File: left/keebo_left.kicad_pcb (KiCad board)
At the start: 2 copper layers, 147.6 x 114.3 mm, 58 parts, among them SW1 SW_Push, SW10 SW_Push, SW11 SW_Push, SW12 SW_Push, SW13 SW_Push, SW14 SW_Push, SW17 SW_Push, SW18 SW_Push, SW19 SW_Push, SW2 SW_Push, SW20 SW_Push, SW21 SW_Push, SW22 SW_Push, SW25 SW_Push, SW26 SW_Push, SW27 SW_Push, SW28 SW_Push, SW29 SW_Push, SW3 SW_Push, SW30 SW_Push, SW34 SW_Push, SW35 SW_Push, SW36 SW_Push, SW4 SW_Push, SW5 SW_Push, SW6 SW_Push, SW7 SW_Push, SW9 SW_Push, U1 nRF24L01_module, U2 keyplus_mini

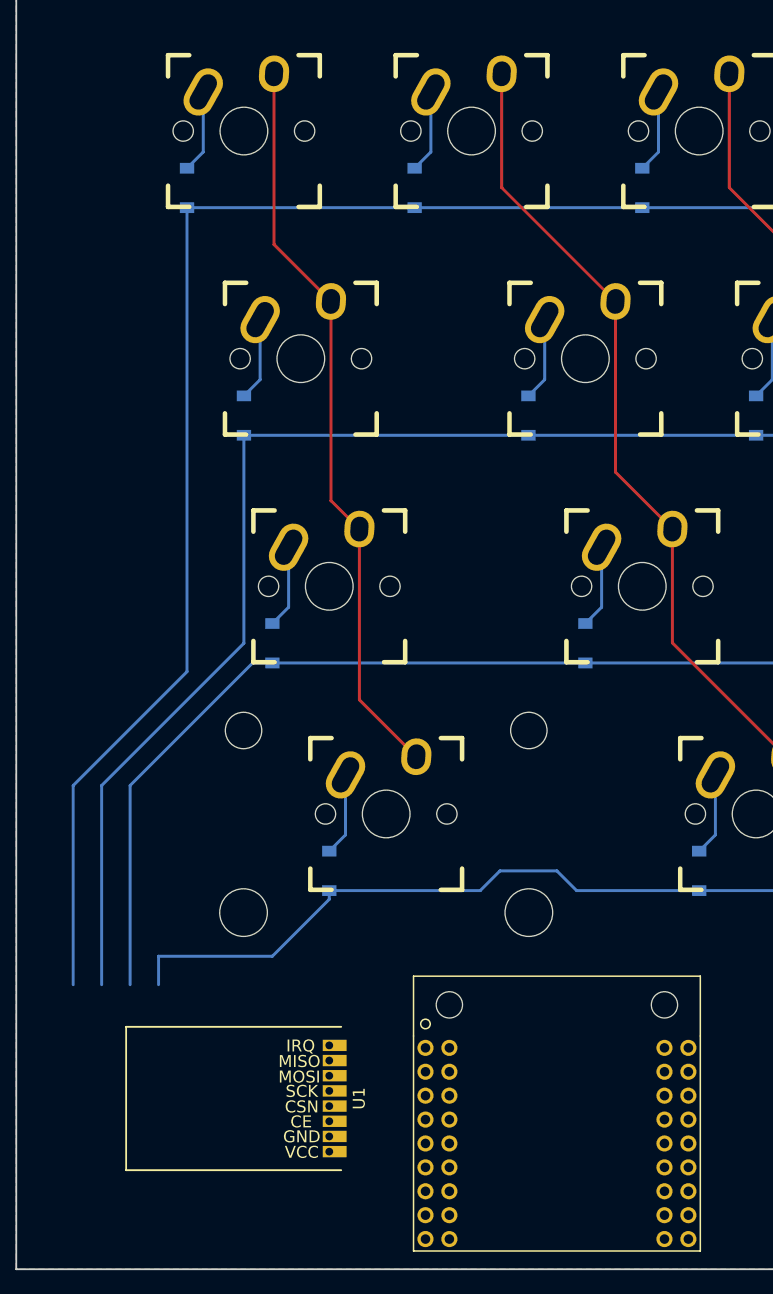
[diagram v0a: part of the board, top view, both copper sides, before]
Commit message: Make dependencies use relative path
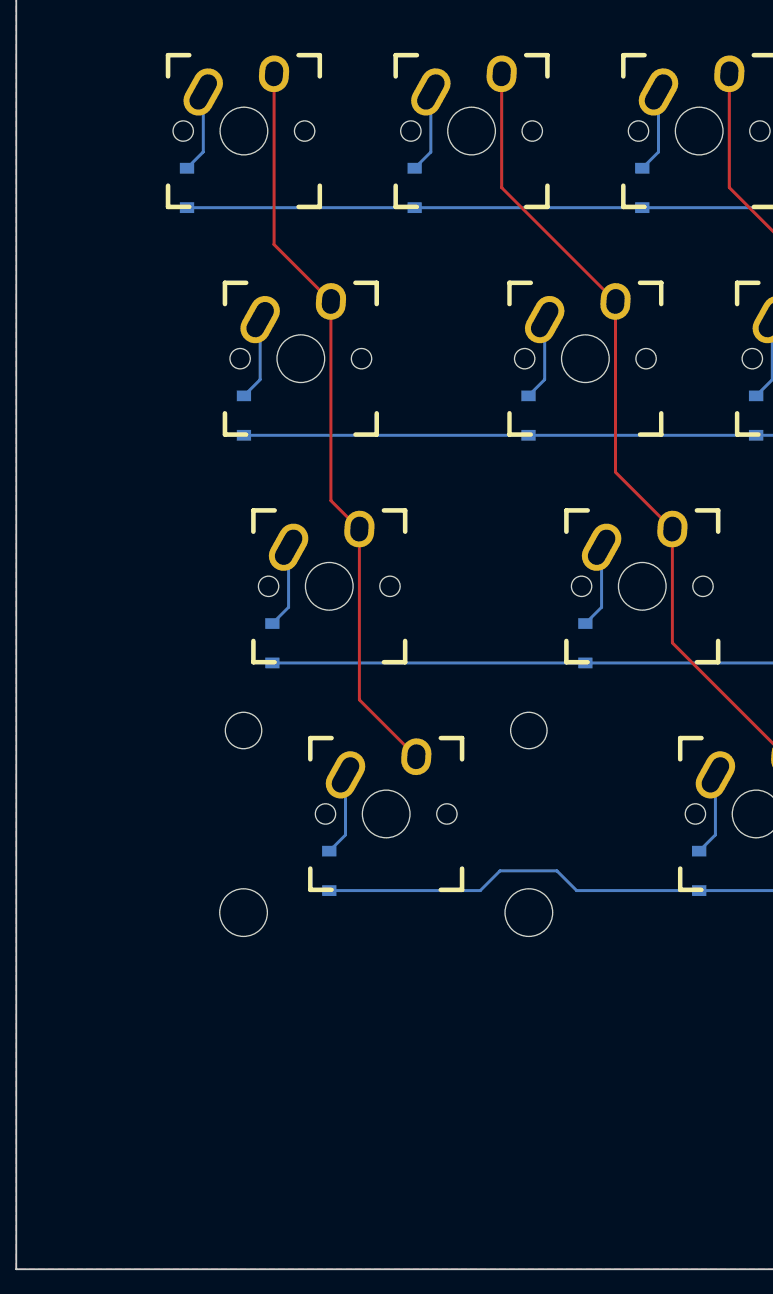
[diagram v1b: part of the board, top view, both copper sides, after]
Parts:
- removed U1: nRF24L01_module, nordic:NRF24L01-Module-SMD-TH
- removed U2: keyplus_mini, keyplus:keyplus_mini_v3
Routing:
- net /row0: track 183.3 -> 114.3 mm
- net /row1: track 150.9 -> 100.0 mm
- net /row2: track 135.2 -> 102.4 mm
- net /row3: track 127.9 -> 108.5 mm

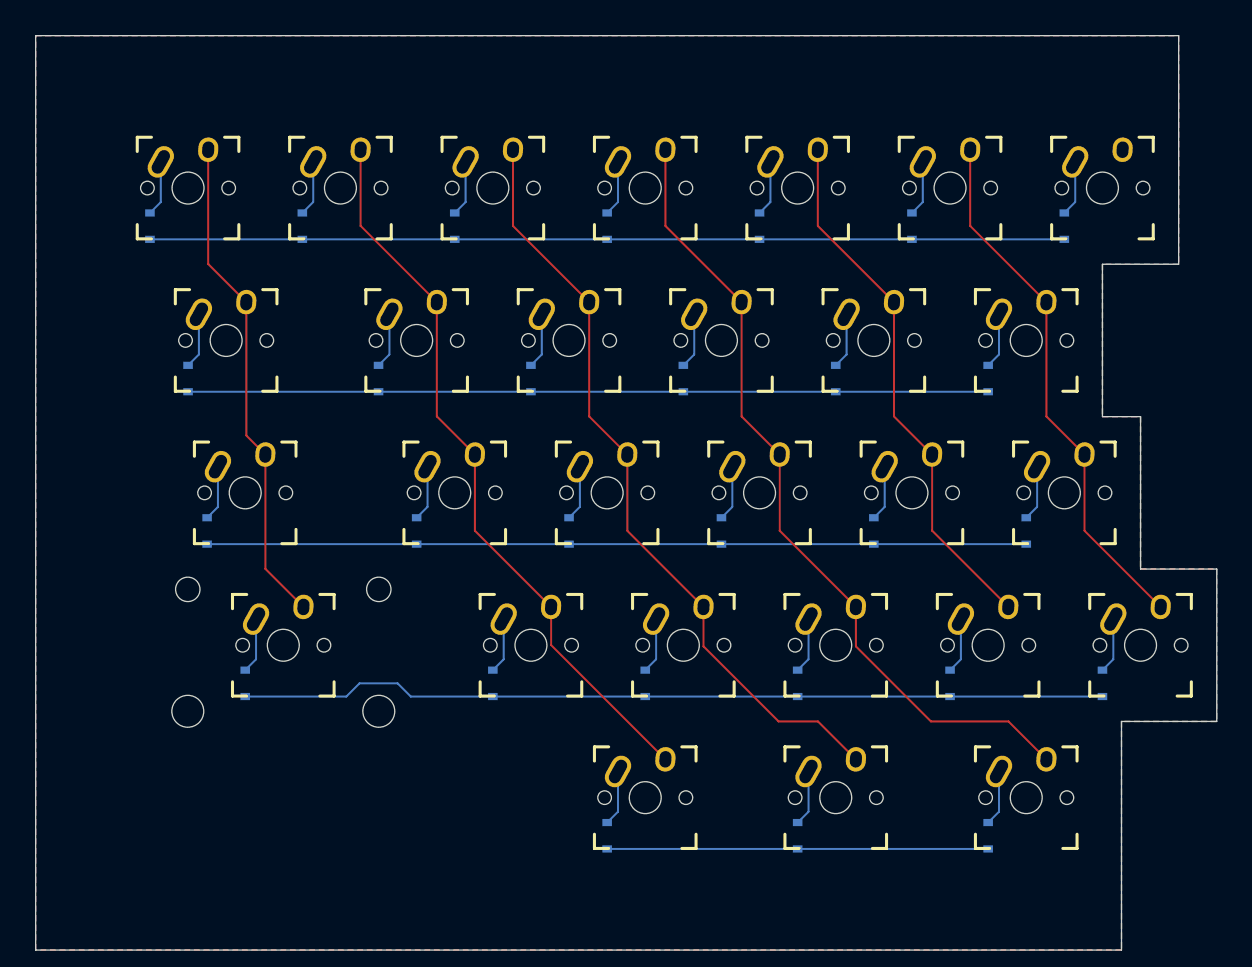
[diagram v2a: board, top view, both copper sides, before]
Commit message: Create PCB for low profile switches
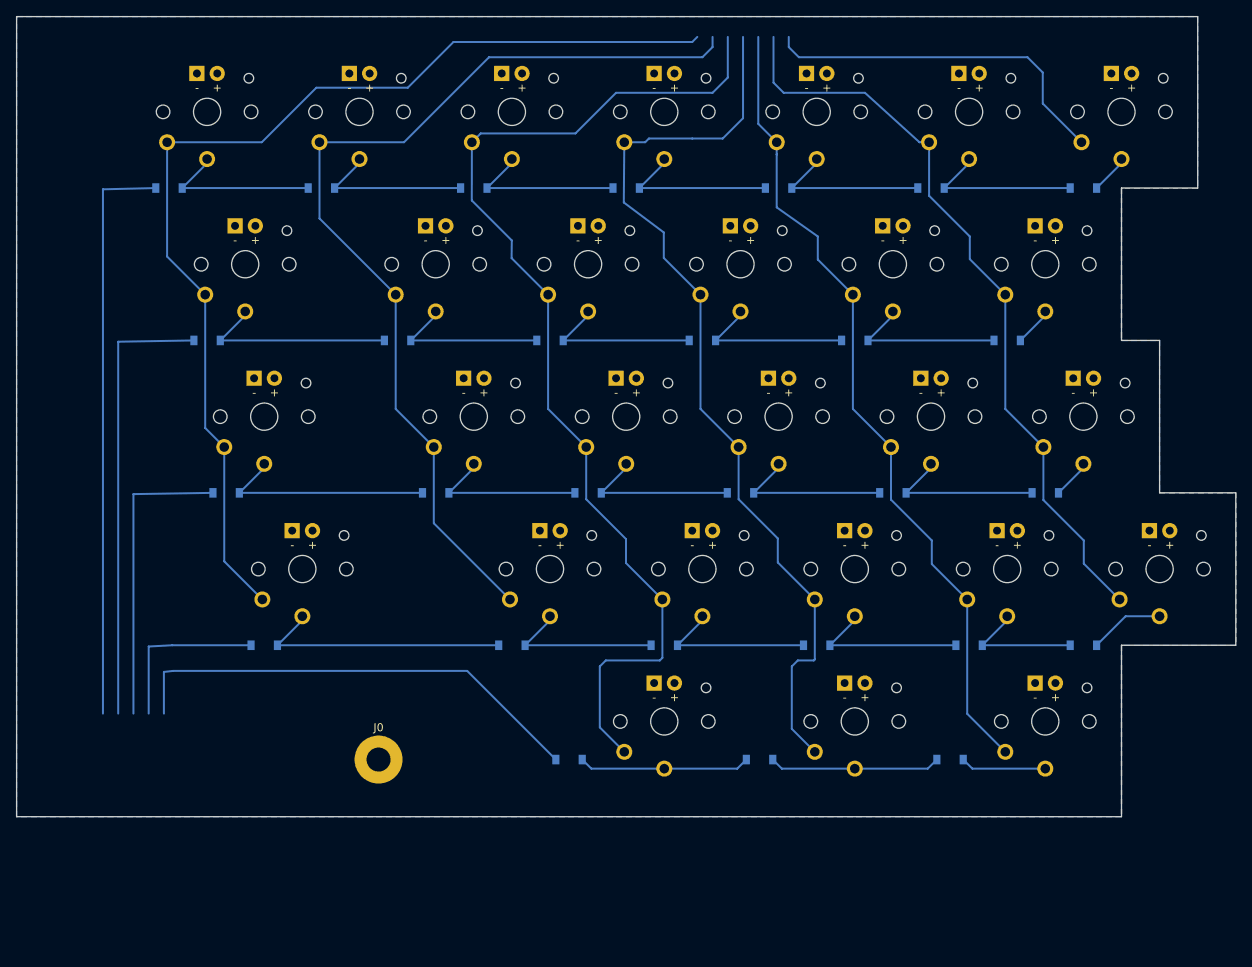
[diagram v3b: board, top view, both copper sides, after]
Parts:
- removed D34: 1N4148, Diodes_SMD:D_SOD-123
- removed SW34: SW_Push, keebs:Mx_Alps_125
- added D37: 1N4148, Diodes_SMD:D_SOD-123, B.Cu at (135.7, 111.9)
- added J0: Conn_01x01, Mounting_Holes:MountingHole_3mm_Pad, F.Cu at (64.3, 111.9)
- added SW37: SW_Push, req:Kailh-PG1350-1u, F.Cu at (147.6, 107.2)
- SW1, SW10, SW11, SW12, SW13, SW14, SW18, SW19, SW2, SW20, SW21, SW22, SW26, SW27, SW28, SW29, SW3, SW30, SW4, SW5, SW6, SW7: footprint keebs:Mx_Alps_100 -> req:Kailh-PG1350-1u
- SW17: footprint keebs:Mx_Alps_175 -> req:Kailh-PG1350-1u
- SW25: footprint keebs:Mx_Alps_225 -> req:Kailh-PG1350-1u
- SW35, SW36: footprint keebs:Mx_Alps_125 -> req:Kailh-PG1350-1u
- SW9: footprint keebs:Mx_Alps_150 -> req:Kailh-PG1350-1u
- moved D35 30.1 mm to (88.1, 111.9), turned to 0 degrees
- moved D36 30.1 mm to (111.9, 111.9), turned to 0 degrees
- moved SW35 23.5 mm to (100.0, 107.2)
- moved SW36 23.5 mm to (123.8, 107.2)
- moved SW6 9.82 mm to (138.1, 31.0)
- moved SW3 9.82 mm to (81.0, 31.0)
- moved SW4 9.82 mm to (100.0, 31.0)
- moved SW13 9.82 mm to (128.6, 50.0)
- moved SW2 9.82 mm to (61.9, 31.0)
- moved SW1 9.82 mm to (42.9, 31.0)
- moved SW5 9.82 mm to (119.1, 31.0)
- moved SW7 9.82 mm to (157.2, 31.0)
- moved SW30 9.82 mm to (161.9, 88.1)
- moved SW9 9.82 mm to (47.6, 50.0)
- moved SW10 9.82 mm to (71.4, 50.0)
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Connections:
- D1 pad 1: /row0 -> (no net)
- D10 pad 1: /row1 -> Net-(D10-Pad1)
- D11 pad 1: /row1 -> Net-(D10-Pad2)
- D12 pad 1: /row1 -> Net-(D11-Pad2)
- D13 pad 1: /row1 -> Net-(D12-Pad2)
- D14 pad 1: /row1 -> Net-(D13-Pad2)
- D17 pad 1: /row2 -> (no net)
- D18 pad 1: /row2 -> Net-(D17-Pad2)
- D19 pad 1: /row2 -> Net-(D18-Pad2)
- D2 pad 1: /row0 -> Net-(D1-Pad2)
- D20 pad 1: /row2 -> Net-(D19-Pad2)
- D21 pad 1: /row2 -> Net-(D20-Pad2)
- D22 pad 1: /row2 -> Net-(D21-Pad2)
- D25 pad 1: /row3 -> (no net)
- D26 pad 1: /row3 -> Net-(D25-Pad2)
- D27 pad 1: /row3 -> Net-(D26-Pad2)
- D28 pad 1: /row3 -> Net-(D27-Pad2)
- D29 pad 1: /row3 -> Net-(D28-Pad2)
- D3 pad 1: /row0 -> Net-(D2-Pad2)
- D30 pad 1: /row3 -> Net-(D29-Pad2)
- D35 pad 1: /row4 -> (no net)
- D36 pad 1: /row4 -> Net-(D35-Pad2)
- D4 pad 1: /row0 -> Net-(D3-Pad2)
- D5 pad 1: /row0 -> Net-(D4-Pad2)
- D6 pad 1: /row0 -> Net-(D5-Pad2)
- D7 pad 1: /row0 -> Net-(D6-Pad2)
- D9 pad 1: /row1 -> (no net)
- D9 pad 2: Net-(D9-Pad2) -> Net-(D10-Pad1)
- SW7 pad 2: /col6 -> (no net)
- SW9 pad 1: Net-(D9-Pad2) -> Net-(D10-Pad1)
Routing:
- net (no net): track 0.00 -> 290.5 mm
- net /row0: track 114.3 -> 0.00 mm
- net /row3: track 108.5 -> 0.00 mm
- net /row2: track 102.4 -> 0.00 mm
- net /row1: track 100.0 -> 0.00 mm
- net /col0: track 62.1 -> 133.9 mm
- net /row4: track 47.6 -> 0.00 mm
- net /col2: track 96.8 -> 135.0 mm
- net /col4: track 67.0 -> 102.7 mm
- net /col1: track 92.1 -> 122.3 mm
- net /col5: track 67.0 -> 95.1 mm
- net Net-(D25-Pad2): track 6.94 -> 32.6 mm
- net Net-(D10-Pad1): track 0.00 -> 25.4 mm
- net Net-(D17-Pad2): track 6.94 -> 27.8 mm
- net Net-(D36-Pad2): track 6.94 -> 22.0 mm
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- added copper zone on B.Cu, net /GND
- removed copper zone on B.Cu, net -BATT
- removed copper zone on F.Cu, net -BATT
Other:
- board size 147.6 x 114.3 mm -> 152.4 x 100 mm

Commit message: Begin recreating standard profile layout
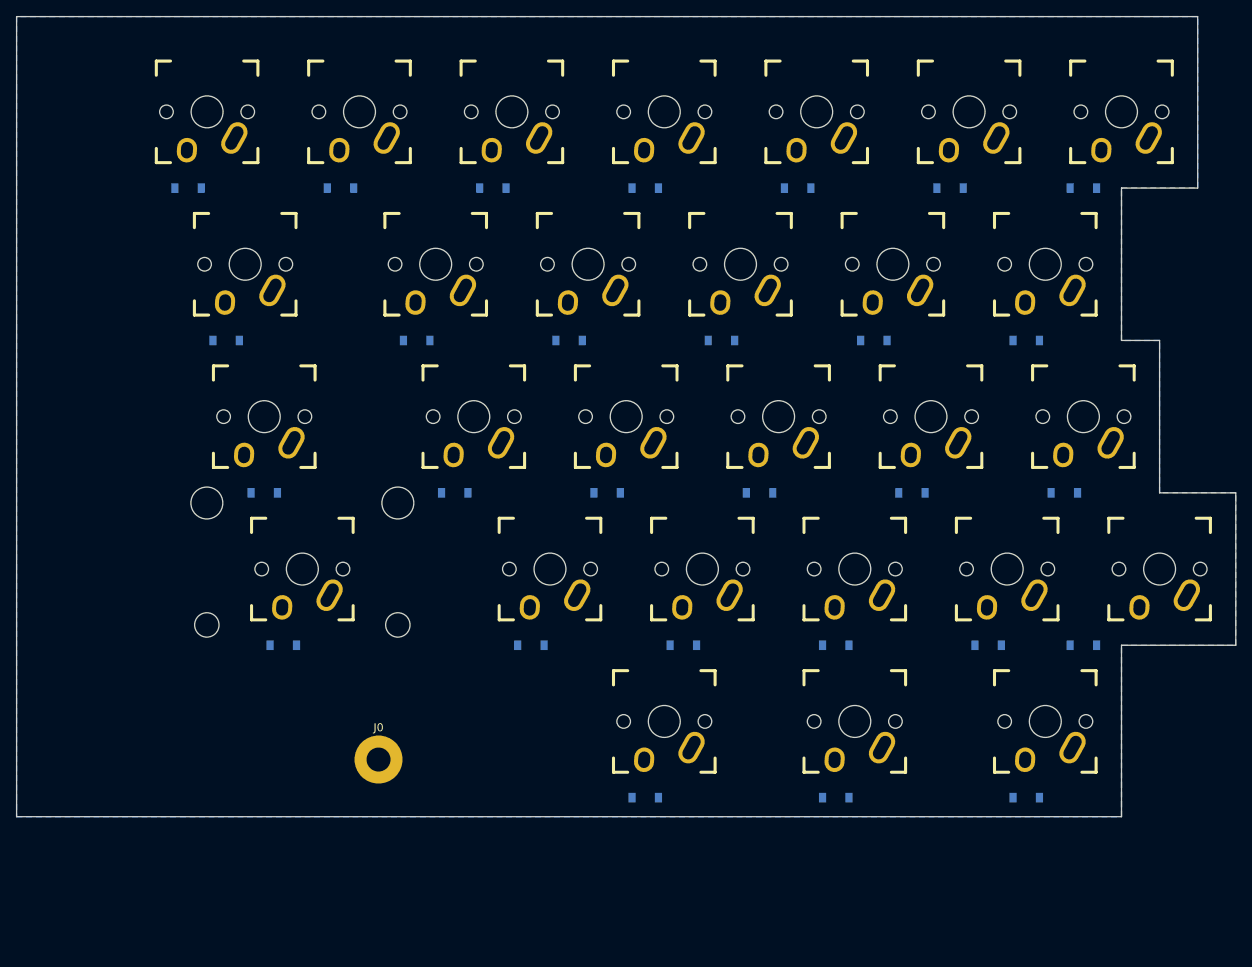
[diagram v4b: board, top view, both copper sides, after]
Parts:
- SW1, SW10, SW11, SW12, SW13, SW14, SW18, SW19, SW2, SW20, SW21, SW22, SW26, SW27, SW28, SW29, SW3, SW30, SW4, SW5, SW6, SW7: footprint req:Kailh-PG1350-1u -> req:Mx_Alps_100
- SW17: footprint req:Kailh-PG1350-1u -> req:Mx_Alps_175
- SW25: footprint req:Kailh-PG1350-1u -> req:Mx_Alps_225
- SW35, SW36, SW37: footprint req:Kailh-PG1350-1u -> req:Mx_Alps_125
- SW9: footprint req:Kailh-PG1350-1u -> req:Mx_Alps_150
- moved D37 10.6 mm to (145.3, 116.7)
- moved D35 10.6 mm to (97.6, 116.7)
- moved D36 10.6 mm to (121.4, 116.7)
- moved D17 4.76 mm to (50.0, 78.6)
- moved D22 2.38 mm to (150.0, 78.6)
- moved D10 2.38 mm to (69.1, 59.5)
- moved D11 2.38 mm to (88.1, 59.5)
- moved D19 2.38 mm to (92.9, 78.6)
- moved D20 2.38 mm to (111.9, 78.6)
- moved D5 2.38 mm to (116.7, 40.5)
- moved D1 2.38 mm to (40.5, 40.5)
- moved D2 2.38 mm to (59.5, 40.5)
- moved D25 2.38 mm to (52.4, 97.6)
- moved D9 2.38 mm to (45.2, 59.5)
- moved D12 2.38 mm to (107.2, 59.5)
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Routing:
- net (no net): track 290.5 -> 0.00 mm
- net /col2: track 135.0 -> 0.00 mm
- net /col0: track 133.9 -> 0.00 mm
- net /col1: track 122.3 -> 0.00 mm
- net /col3: track 116.3 -> 0.00 mm
- net /col4: track 102.7 -> 0.00 mm
- net /col5: track 95.1 -> 0.00 mm
- net Net-(D25-Pad2): track 32.6 -> 0.00 mm
- net Net-(D17-Pad2): track 27.8 -> 0.00 mm
- net Net-(D10-Pad1): track 25.4 -> 0.00 mm
- net Net-(D36-Pad2): track 22.0 -> 0.00 mm
- net Net-(D35-Pad2): track 22.0 -> 0.00 mm
- net Net-(D27-Pad2): track 20.7 -> 0.00 mm
- net Net-(D13-Pad2): track 20.7 -> 0.00 mm
- net Net-(D6-Pad2): track 20.7 -> 0.00 mm
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
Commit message: Create left board using new switch footprints
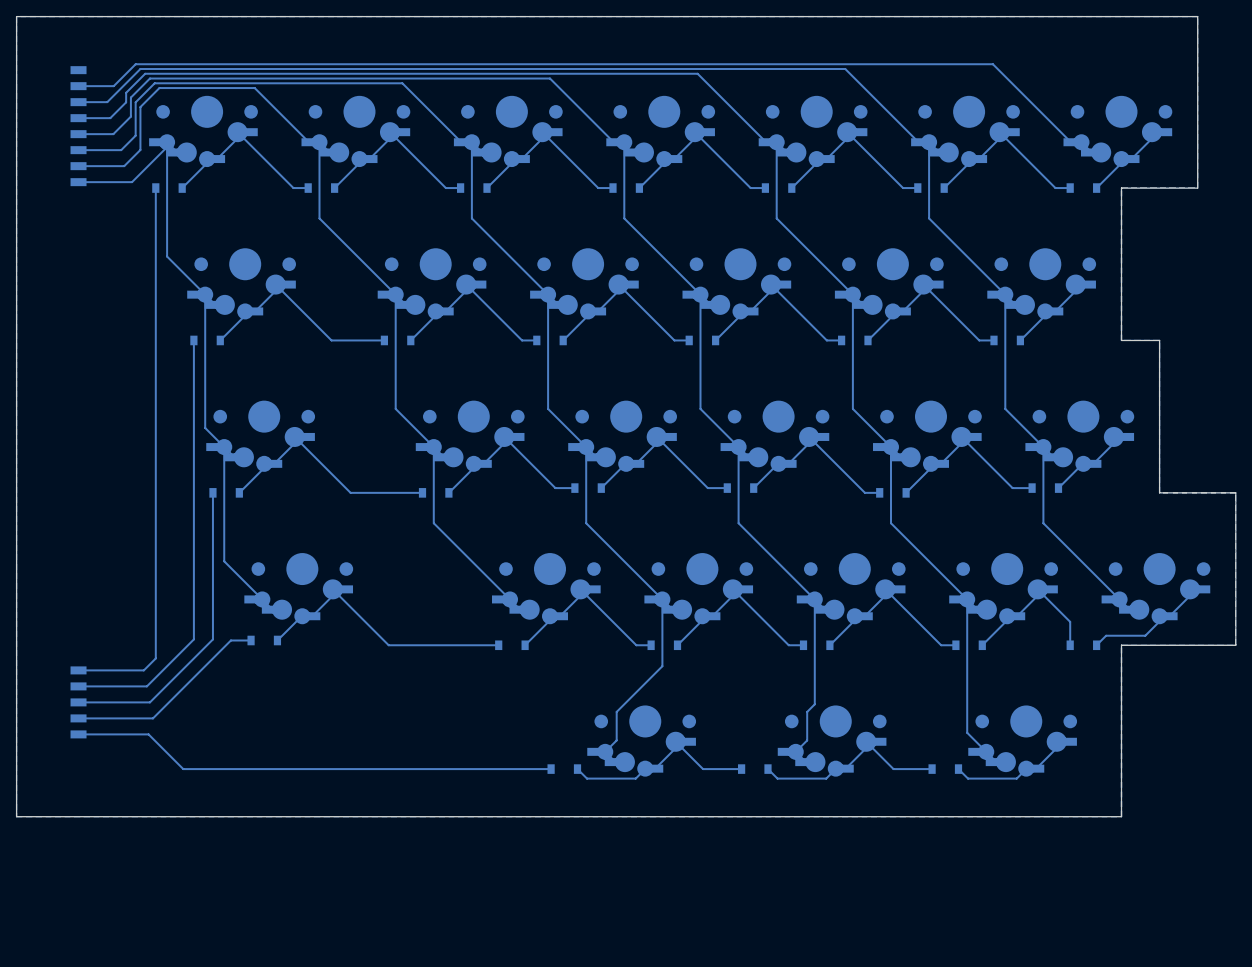
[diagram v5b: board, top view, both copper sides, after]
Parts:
- removed J0: Conn_01x01, Mounting_Holes:MountingHole_3mm_Pad
- added J1: Conn_01x05, kbo_pads:2mm_Pads_01x05, B.Cu at (26.8, 104.8)
- added J2: Conn_01x08, kbo_pads:2mm_Pads_01x08, B.Cu at (26.8, 32.7)
- SW1, SW10, SW11, SW12, SW13, SW14, SW18, SW19, SW2, SW20, SW21, SW22, SW26, SW27, SW28, SW29, SW3, SW30, SW4, SW5, SW6, SW7: footprint req:Mx_Alps_100 -> kbo_mx_lp_3d:KeeboHR_100_MX_LP; moved to B.Cu
- SW17: footprint req:Mx_Alps_175 -> kbo_mx_lp_3d:KeeboHR_175_MX_LP; moved to B.Cu
- SW25: footprint req:Mx_Alps_225 -> kbo_mx_lp_3d:KeeboHR_225_MX_LP; moved to B.Cu
- SW35, SW36, SW37: footprint req:Mx_Alps_125 -> kbo_mx_lp_3d:KeeboHR_125_MX_LP; moved to B.Cu
- SW9: footprint req:Mx_Alps_150 -> kbo_mx_lp_3d:KeeboHR_150_MX_LP; moved to B.Cu
- moved D37 10.7 mm to (135.1, 113.1)
- moved D35 10.7 mm to (87.5, 113.1)
- moved D36 10.7 mm to (111.3, 113.1)
- moved D17 4.76 mm to (45.2, 78.6)
- moved D22 2.45 mm to (147.6, 78.0)
- moved D19 2.45 mm to (90.5, 78.0)
- moved D20 2.45 mm to (109.5, 78.0)
- moved D25 2.45 mm to (50.0, 97.0)
- moved D29 2.38 mm to (138.1, 97.6)
- moved D1 2.38 mm to (38.1, 40.5)
- moved D10 2.38 mm to (66.7, 59.5)
- moved D11 2.38 mm to (85.7, 59.5)
- moved D12 2.38 mm to (104.8, 59.5)
- moved D13 2.38 mm to (123.8, 59.5)
- moved D2 2.38 mm to (57.2, 40.5)
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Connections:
- D1 pad 1: (no net) -> /row1
- D17 pad 1: (no net) -> /row3
- D25 pad 1: (no net) -> /row4
- D35 pad 1: (no net) -> /row5
- D9 pad 1: (no net) -> /row2
- SW1 pad 2: /col0 -> /col1
- SW10 pad 2: /col1 -> /col2
- SW11 pad 2: /col2 -> /col3
- SW12 pad 2: /col3 -> /col4
- SW13 pad 2: /col4 -> /col5
- SW14 pad 2: /col5 -> /col6
- SW17 pad 2: /col0 -> /col1
- SW18 pad 2: /col1 -> /col2
- SW19 pad 2: /col2 -> /col3
- SW2 pad 2: /col1 -> /col2
- SW20 pad 2: /col3 -> /col4
- SW21 pad 2: /col4 -> /col5
- SW22 pad 2: /col5 -> /col6
- SW25 pad 2: /col0 -> /col1
- SW26 pad 2: /col1 -> /col2
- SW27 pad 2: /col2 -> /col3
- SW28 pad 2: /col3 -> /col4
- SW29 pad 2: /col4 -> /col5
- SW3 pad 2: /col2 -> /col3
- SW30 pad 2: /col5 -> /col6
- SW35 pad 2: /col2 -> /col3
- SW36 pad 2: /col3 -> /col4
- SW37 pad 2: /col4 -> /col5
- SW4 pad 2: /col3 -> /col4
- SW5 pad 2: /col4 -> /col5
- SW6 pad 2: /col5 -> /col6
- SW7 pad 2: (no net) -> /col7
- SW9 pad 2: /col0 -> /col1
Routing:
- net /col5: track 0.00 -> 203.1 mm
- net /col6: track 0.00 -> 196.5 mm
- net /col4: track 0.00 -> 184.0 mm
- net /col3: track 0.00 -> 168.4 mm
- net /col7: track 0.00 -> 135.5 mm
- net /col2: track 0.00 -> 124.1 mm
- net /col1: track 0.00 -> 92.5 mm
- net /row1: track 0.00 -> 69.1 mm
- net /row5: track 0.00 -> 60.9 mm
- net /row2: track 0.00 -> 54.2 mm
- net /row3: track 0.00 -> 38.4 mm
- net Net-(D25-Pad2): track 0.00 -> 35.2 mm
- net Net-(D17-Pad2): track 0.00 -> 31.0 mm
- net Net-(D10-Pad1): track 0.00 -> 28.6 mm
- net Net-(D36-Pad2): track 0.00 -> 26.9 mm
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- added copper zone on B.Cu, net (none)
- removed copper zone on B.Cu, net /GND
